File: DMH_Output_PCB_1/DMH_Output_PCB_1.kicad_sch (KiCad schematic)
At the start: 0 parts

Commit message: Schematic in progress
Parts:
- added J1, J2: TS_Jack_6.35mm_Sw, SynthStuff:CUI_MJ-63052A, symbol SynthStuff:TS_Jack_6.35mm_Sw
- added J200: IDC_02x05, SynthStuff:IDC-Header_2x05_P2.54mm_Vertical_BackBone, symbol SynthStuff:BackBone_Connector_10Pin
- added J3, J4, J5: AudioJack3, symbol Connector_Audio:AudioJack3
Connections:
- new net Balanced Line Driver/L_Bal_OUT_N: J3.R
- new net Balanced Line Driver/L_Bal_OUT_P: J3.T
- new net Balanced Line Driver/R_Bal_OUT_N: J4.R
- new net Balanced Line Driver/R_Bal_OUT_P: J4.T
- new net GND: J1.S, J2.S, J3.S, J4.S, J5.S
- new net Headphone Amplifier/L_HP_OUT: J5.T
- new net Headphone Amplifier/R_HP_OUT: J5.R
- new net Pre-Gain Stage/Left_In: J1.T
- new net Pre-Gain Stage/Right In: J2.T
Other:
- removed sheet Core Circuit
- removed sheet Inputs and Outputs
- added sheet Balanced Line Driver (Balanced_line_driver.kicad_sch)
- added sheet Gain Trimmer (Gain_trimmer.kicad_sch)
- added sheet Headphone Amplifier (Headphone_amplifier.kicad_sch)
- added sheet Pre-Gain Stage (Pregain_stage.kicad_sch)

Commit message: PreAmp design starting
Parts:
- added J6, J7, J8, J9: TS_Jack_6.35mm_Sw, SynthStuff:CUI_MJ-63052A, symbol SynthStuff:TS_Jack_6.35mm_Sw
- J1: Function Input L -> In L
- J2: Function Input R -> In R
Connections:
- net GND: now also J6.S, J7.S, J8.S, J9.S
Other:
- added sheet PreAmp (PreAmp.kicad_sch)
- sheet Meter ports: added Meter Left, Meter Right; removed none
- moved on the sheet: J5

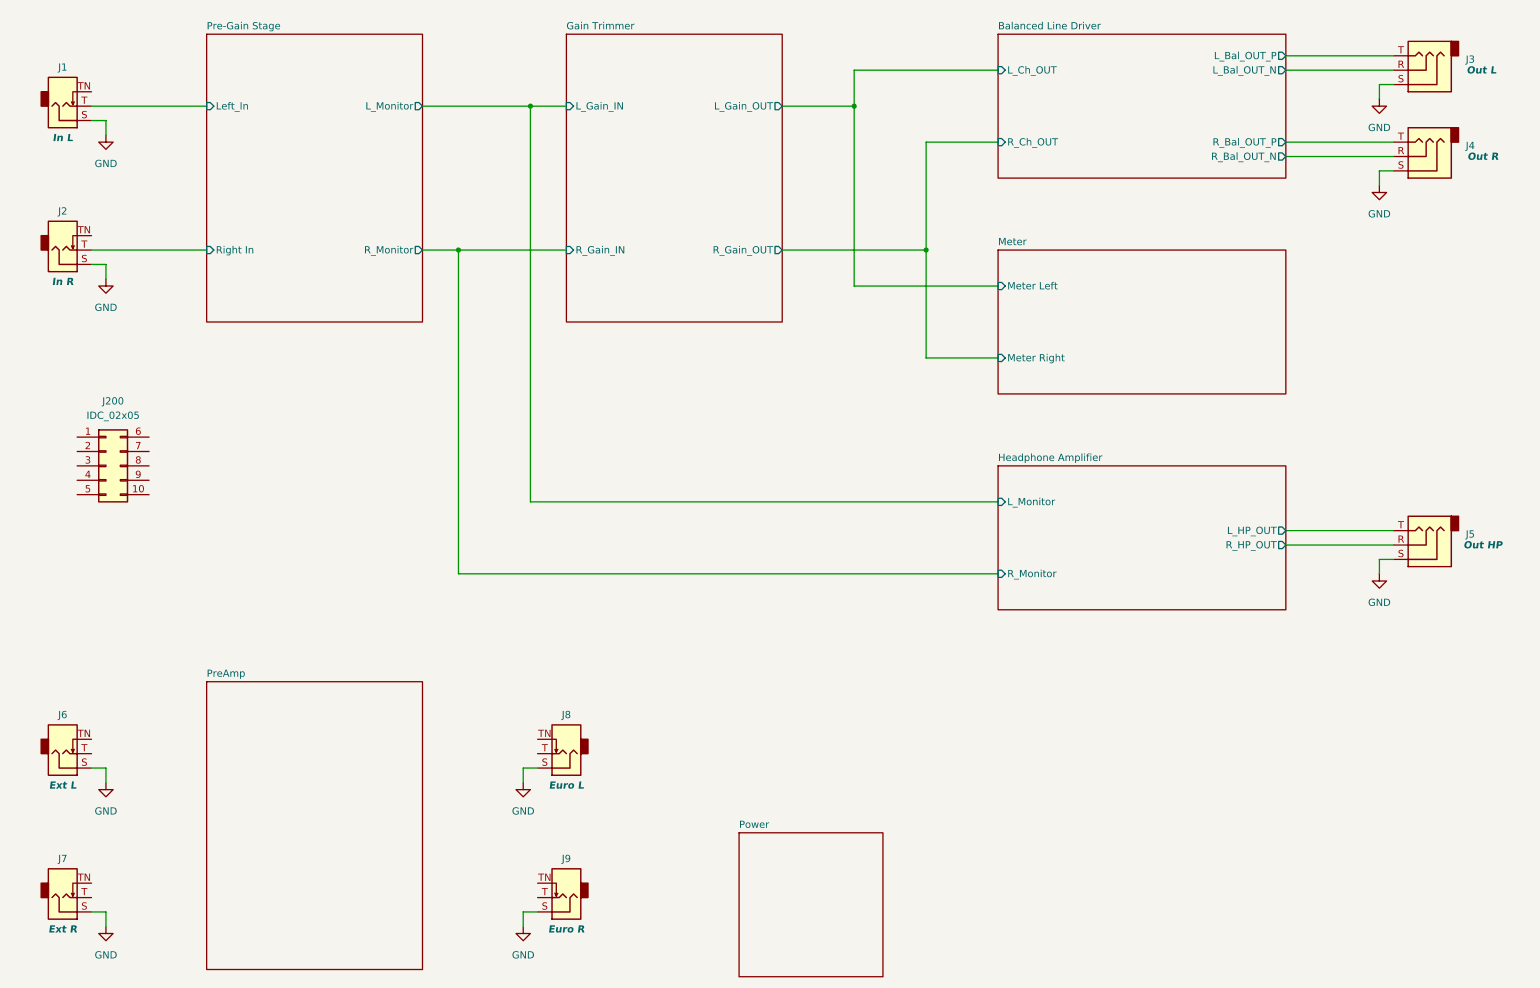
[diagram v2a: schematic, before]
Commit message: Designed preamp circuit
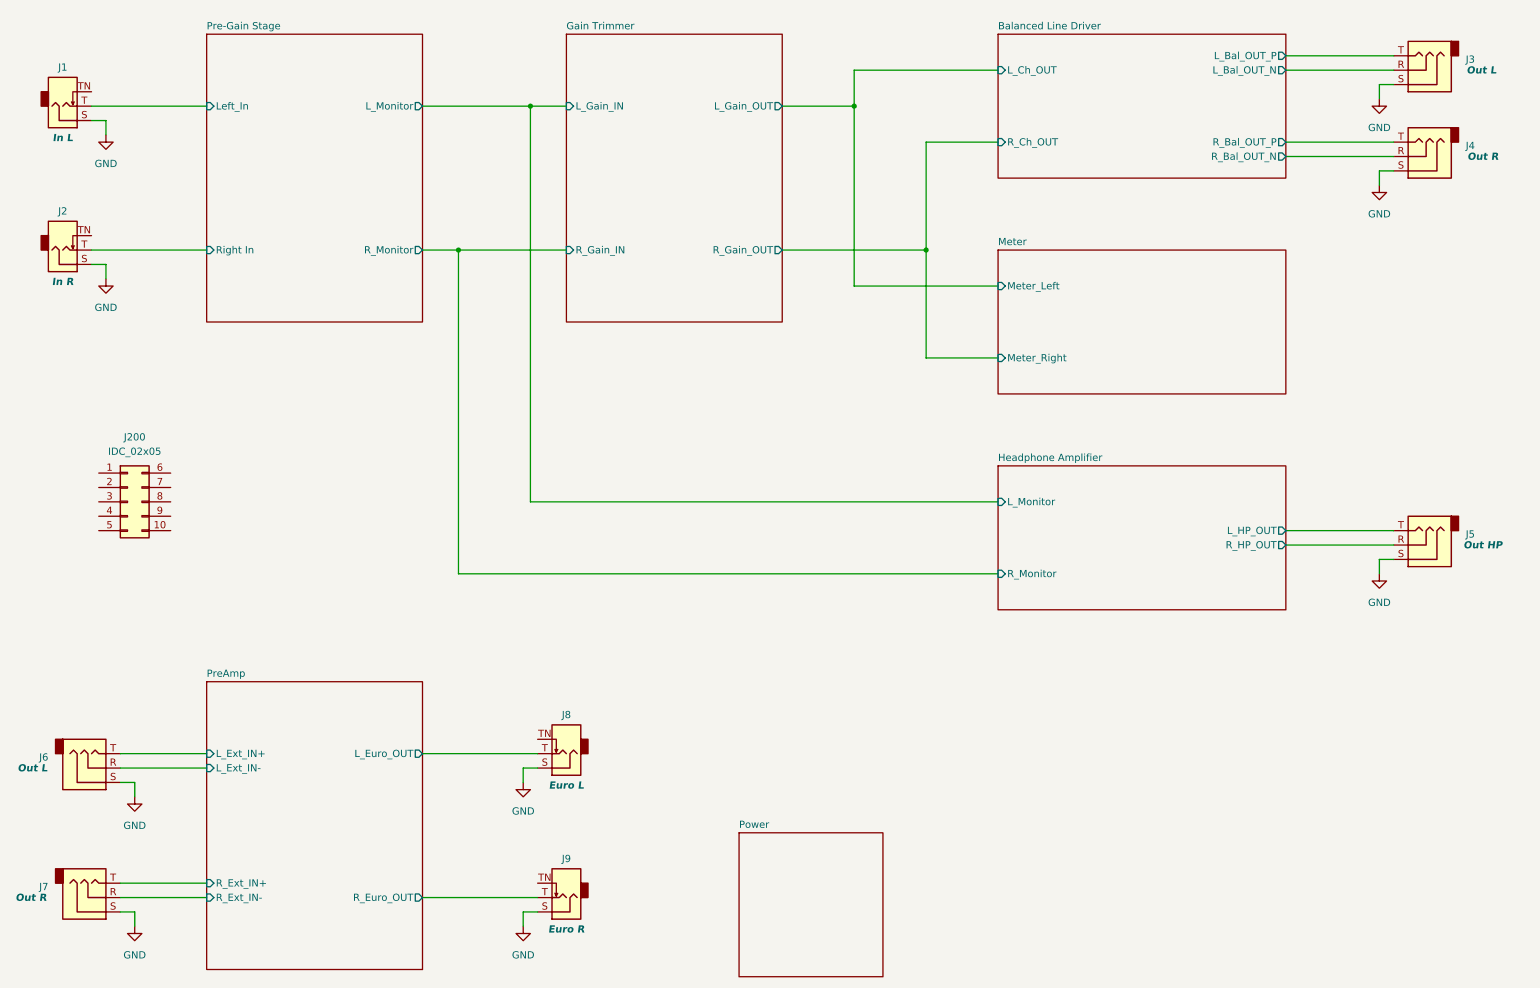
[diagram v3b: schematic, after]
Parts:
- removed J6, J7: TS_Jack_6.35mm_Sw, SynthStuff:CUI_MJ-63052A, symbol SynthStuff:TS_Jack_6.35mm_Sw
- added J6, J7: AudioJack3, symbol Connector_Audio:AudioJack3
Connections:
- net GND: now also J6.S, J7.S
- net PreAmp/L_Euro_OUT: now reaches J8.T
- net PreAmp/R_Euro_OUT: now reaches J9.T
- new net PreAmp/L_Ext_IN+: J6.T
- new net PreAmp/L_Ext_IN-: J6.R
- new net PreAmp/R_Ext_IN+: J7.T
- new net PreAmp/R_Ext_IN-: J7.R
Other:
- sheet Meter ports: added Meter_Left, Meter_Right; removed Meter Left, Meter Right
- sheet PreAmp ports: added L_Euro_OUT, L_Ext_IN+, L_Ext_IN-, R_Euro_OUT, R_Ext_IN+, R_Ext_IN-; removed none
- moved on the sheet: J200

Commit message: Designed external input meter
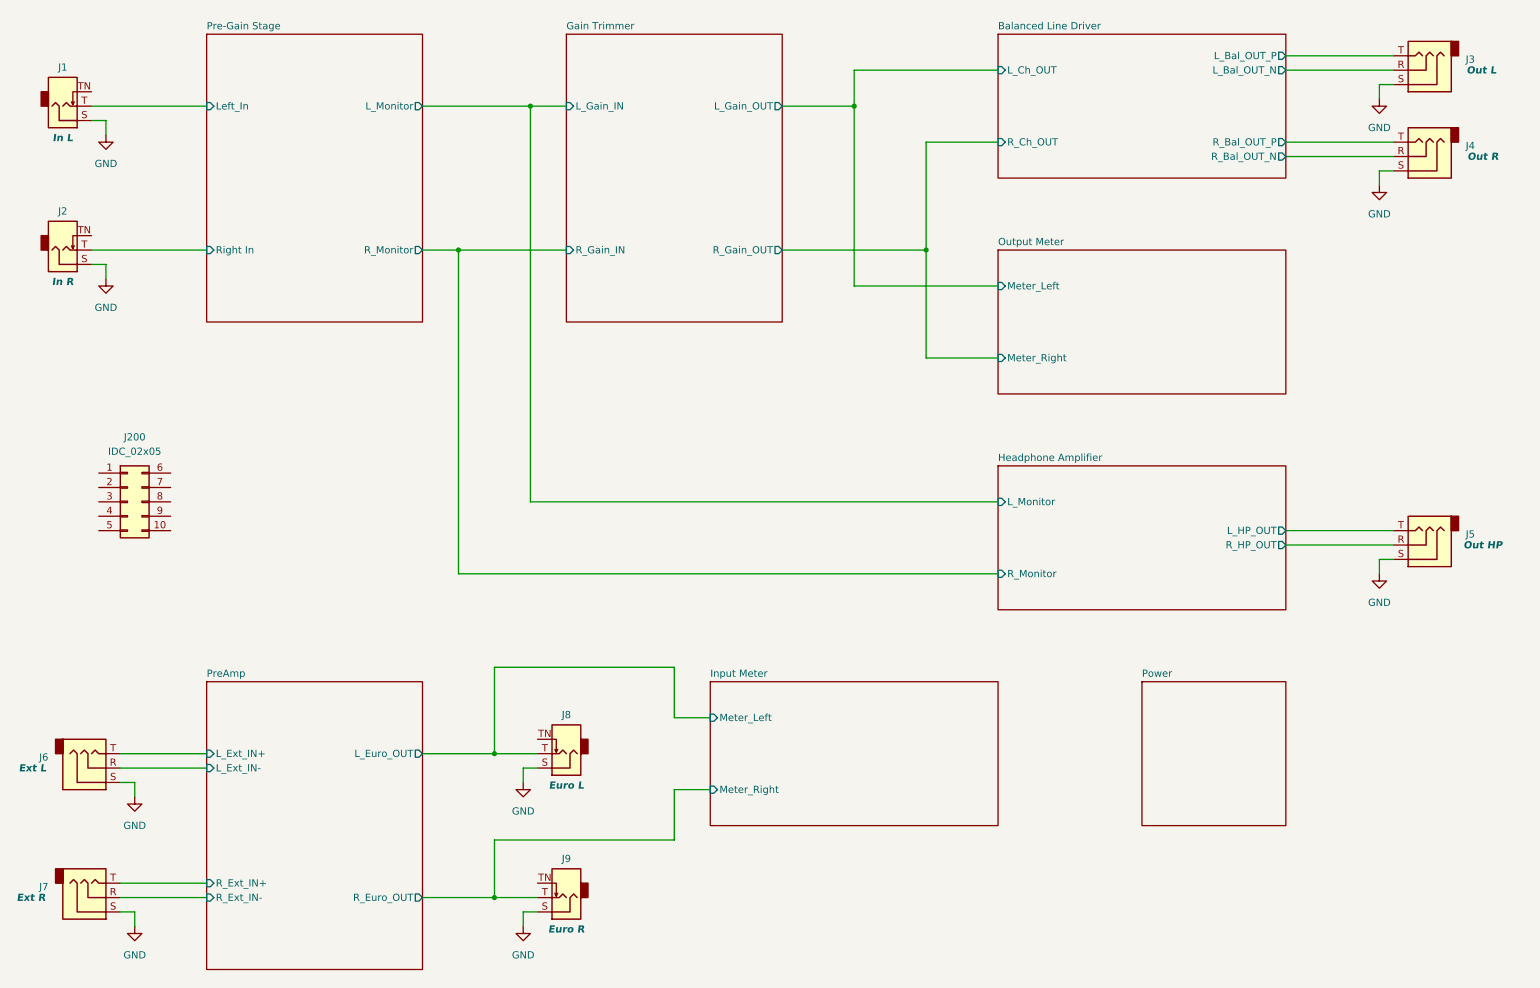
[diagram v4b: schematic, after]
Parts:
- J6: Function Out L -> Ext L
- J7: Function Out R -> Ext R
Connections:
- net PreAmp/L_Euro_OUT renamed Input Meter/Meter_Left
- net PreAmp/R_Euro_OUT renamed Input Meter/Meter_Right
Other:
- sheet Meter renamed Output Meter
- added sheet Input Meter (Input_Meter.kicad_sch)
- sheet Output Meter: file Meter.kicad_sch -> Output_Meter.kicad_sch

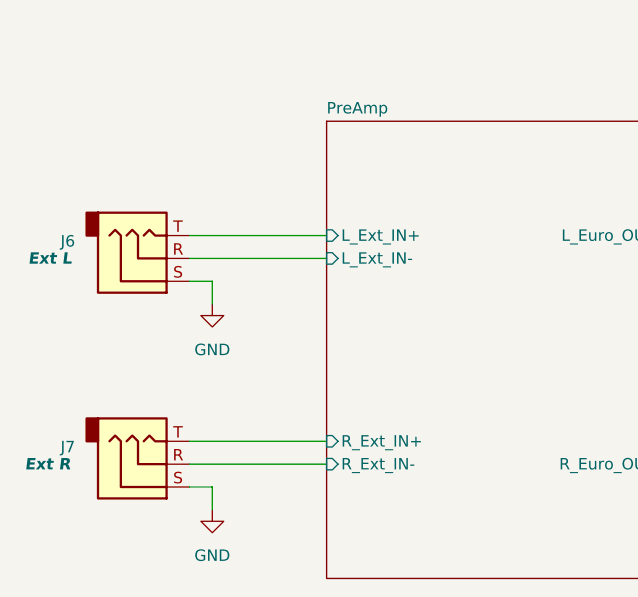
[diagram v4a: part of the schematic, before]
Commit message: Redesigned external input preamp
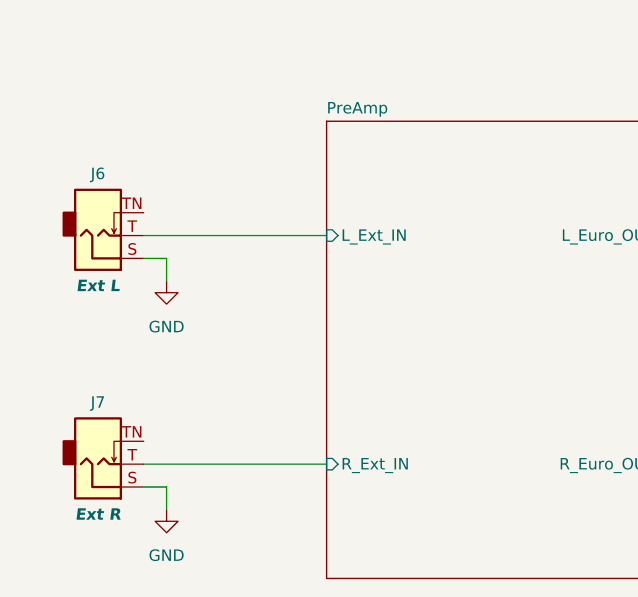
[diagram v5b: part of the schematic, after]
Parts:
- removed J6, J7: AudioJack3, symbol Connector_Audio:AudioJack3
- added J6, J7: TS_Jack_6.35mm_Sw, SynthStuff:CUI_MJ-63052A, symbol SynthStuff:TS_Jack_6.35mm_Sw
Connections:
- net GND: now also J6.S, J7.S
- new net PreAmp/L_Ext_IN: J6.T
- new net PreAmp/R_Ext_IN: J7.T
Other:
- sheet PreAmp ports: added L_Ext_IN, R_Ext_IN; removed L_Ext_IN+, L_Ext_IN-, R_Ext_IN+, R_Ext_IN-

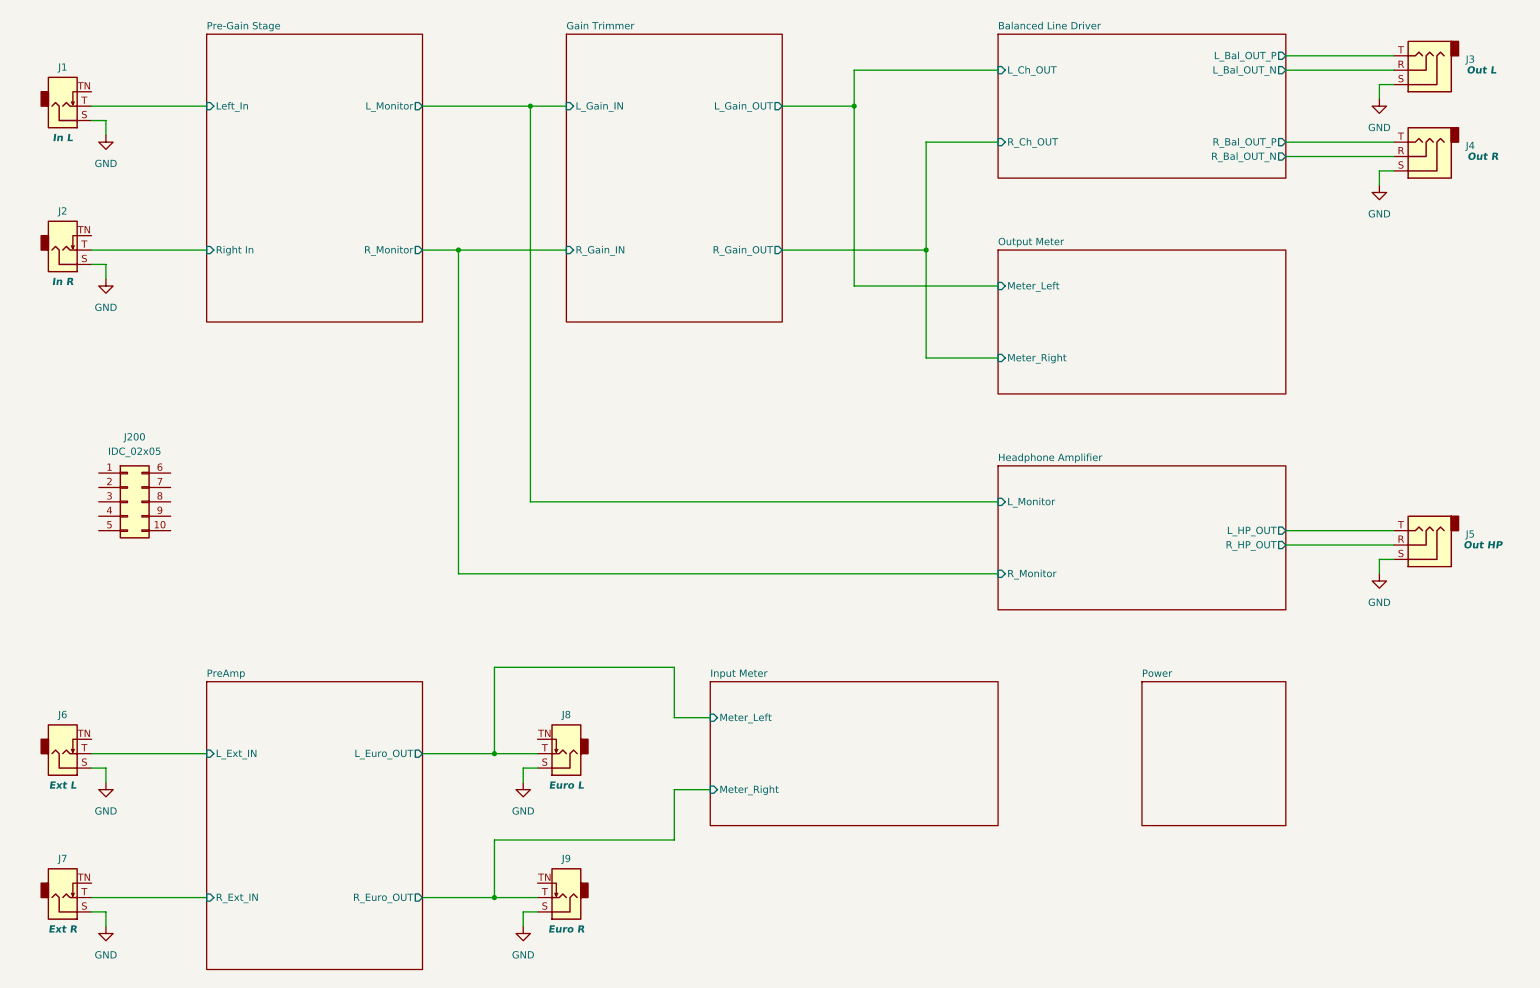
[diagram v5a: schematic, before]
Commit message: Updated meters resistor values
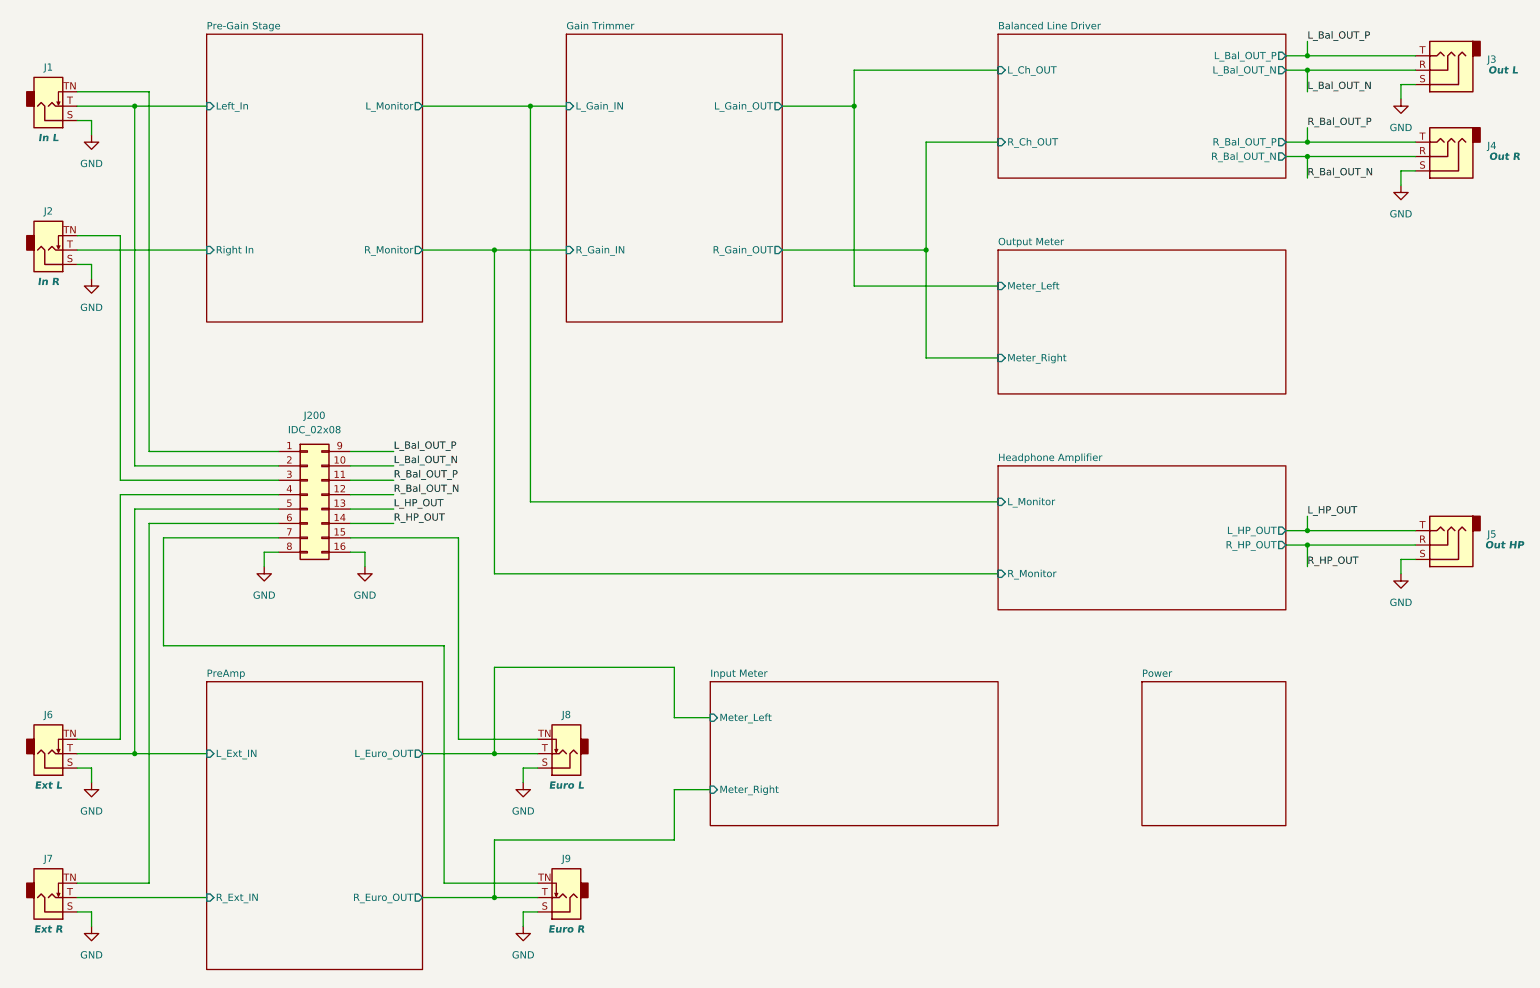
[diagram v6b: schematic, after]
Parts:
- J200: value IDC_02x05 -> IDC_02x08; footprint SynthStuff:IDC-Header_2x05_P2.54mm_Vertical_BackBone -> SynthStuff:IDC-Header_2x08_P2.54mm_Vertical_BackBone; symbol SynthStuff:BackBone_Connector_10Pin -> SynthStuff:BackBone_Connector_16Pin
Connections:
- net Balanced Line Driver/L_Bal_OUT_N is gone; now on net L_Bal_OUT_N: J3.R
- net Balanced Line Driver/L_Bal_OUT_P is gone; now on net L_Bal_OUT_P: J3.T
- net GND: now also J200.16 (Pin_16), J200.8 (Pin_8)
- net Pre-Gain Stage/Left_In: now also J200.2 (Pin_2)
- net PreAmp/L_Ext_IN: now also J200.5 (Pin_5)
- net at J8.TN: now also J200.15 (Pin_15)
- net at J2.TN: now also J200.3 (Pin_3)
- net at J7.TN: now also J200.6 (Pin_6)
- net at J6.TN: now also J200.4 (Pin_4)
- net at J200.1 (Pin_1): now also J1.TN
- net L_Bal_OUT_N: now reaches J200.10 (Pin_10)
- net at J200.7 (Pin_7): now also J9.TN
- net L_Bal_OUT_P: now reaches J200.9 (Pin_9)
- net Balanced Line Driver/R_Bal_OUT_N renamed R_Bal_OUT_N
- net R_Bal_OUT_N: now also J200.12 (Pin_12)
- net Balanced Line Driver/R_Bal_OUT_P renamed R_Bal_OUT_P
- net R_Bal_OUT_P: now also J200.11 (Pin_11)
- net Headphone Amplifier/L_HP_OUT renamed L_HP_OUT
- net L_HP_OUT: now also J200.13 (Pin_13)
- net Headphone Amplifier/R_HP_OUT renamed R_HP_OUT
- net R_HP_OUT: now also J200.14 (Pin_14)
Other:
- moved on the sheet: J1, J2, J3, J4, J5, J6, J7

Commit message: Linked TRS jacks footprint
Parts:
- J3, J4, J5: value AudioJack3 -> TRS Jack 6.35mm; footprint (none) -> SynthStuff:CUI_SJ-63083A
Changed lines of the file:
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@@
 			)
 		)
-		(property "Value" "AudioJack3"
+		(property "Value" "TRS Jack 6.35mm"
 			(at 276.86 47.6249 0)
 			(effects
@@
 			)
 		)
-		(property "Footprint" ""
+		(property "Footprint" "SynthStuff:CUI_SJ-63083A"
 			(at 269.24 46.99 0)
 			(effects
@@
 			)
 		)
-		(property "Value" "AudioJack3"
+		(property "Value" "TRS Jack 6.35mm"
 			(at 276.86 116.2049 0)
 			(effects
@@
 			)
 		)
-		(property "Footprint" ""
+		(property "Footprint" "SynthStuff:CUI_SJ-63083A"
 			(at 269.24 115.57 0)
 			(effects
@@
 			)
 		)
-		(property "Value" "AudioJack3"
+		(property "Value" "TRS Jack 6.35mm"
 			(at 276.86 32.3849 0)
 			(effects
@@
 			)
 		)
-		(property "Footprint" ""
+		(property "Footprint" "SynthStuff:CUI_SJ-63083A"
 			(at 269.24 31.75 0)
 			(effects
